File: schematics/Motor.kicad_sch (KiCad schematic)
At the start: 9 parts

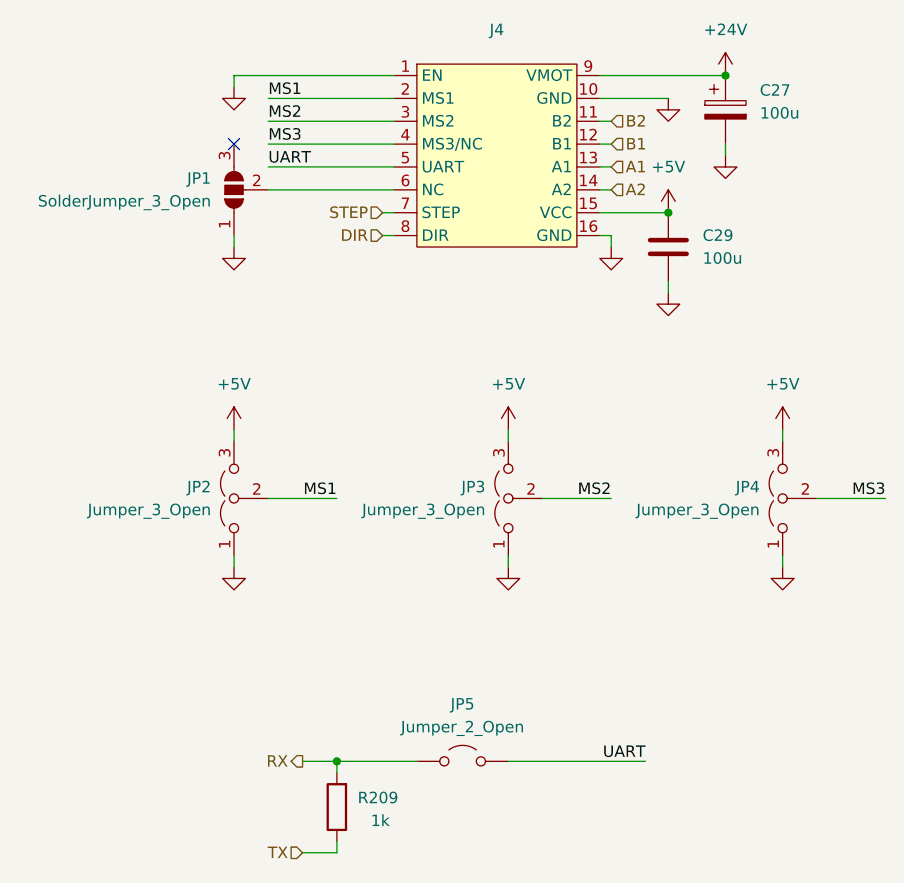
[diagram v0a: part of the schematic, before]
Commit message: Добавил концевик в схему и подправил схему мотора
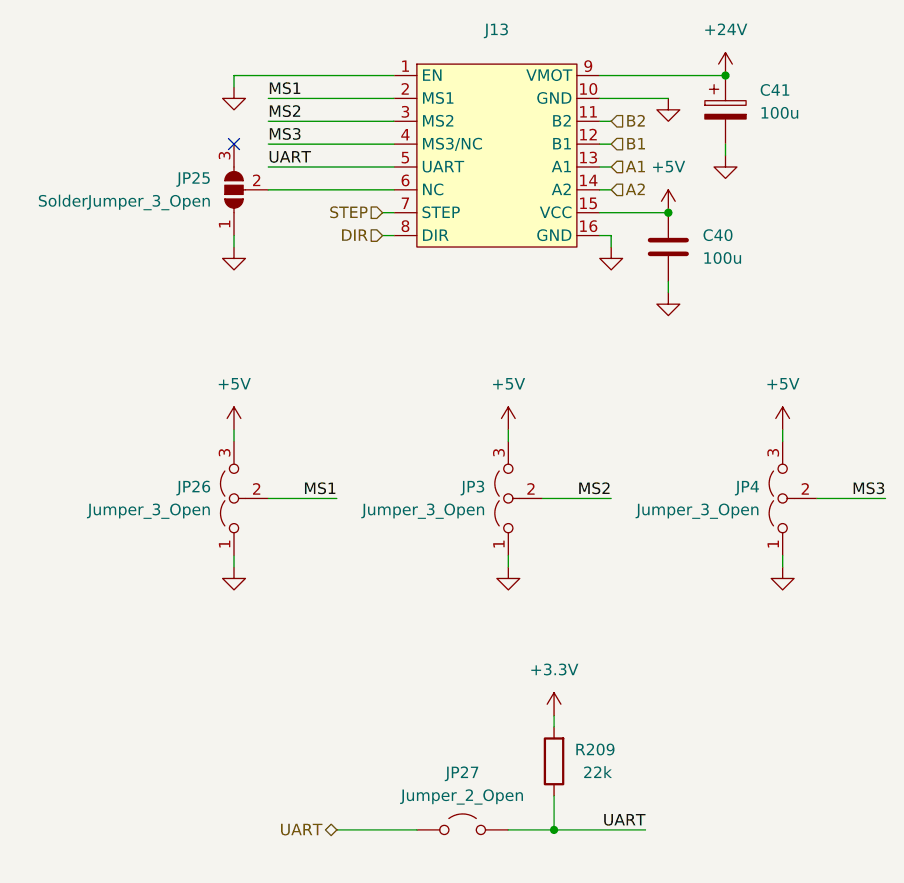
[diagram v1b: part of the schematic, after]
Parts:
- R209: value 1k -> 22k
- renumbered C29 to C40, C27 to C41, J4 to J13, JP1 to JP25, JP2 to JP26, JP5 to JP27
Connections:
- net TX is gone; now on net UART: R209.1
- net UART: now also JP27.1 (A)
- net RX renamed +3.3V
- net +3.3V: no longer JP27.1 (A)
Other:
- moved on the sheet: JP27

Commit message: Файлы измененный Kicad
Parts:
- C40: footprint (none) -> Capacitor_SMD:C_0805_2012Metric
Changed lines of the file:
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@@
 			)
 		)
-		(property "Footprint" ""
+		(property "Footprint" "Capacitor_SMD:C_0805_2012Metric"
 			(at 168.6052 80.01 0)
 			(effects
@@
 		(lib_id "Device:C_Polarized")
 		(at 173.99 60.96 0)
-		(unit 1)
-		(exclude_from_sim no)
-		(in_bom yes)
-		(on_board yes)
-		(dnp no)
-		(fields_autoplaced yes)
+		(mirror y)
+		(unit 1)
+		(exclude_from_sim no)
+		(in_bom yes)
+		(on_board yes)
+		(dnp no)
 		(property "Reference" "C?"
-			(at 177.8 58.8009 0)
+			(at 181.102 58.674 0)
 			(effects
 				(font
@@
 		)
 		(property "Value" "100u"
-			(at 177.8 61.3409 0)
+			(at 182.88 61.468 0)
 			(effects
 				(font
@@
 		)
 		(property "Footprint" "Capacitor_SMD:CP_Elec_6.3x7.7"
-			(at 174.9552 64.77 0)
-			(effects
-				(font
+			(at 173.0248 64.77 0)
+			(effects
+				(font

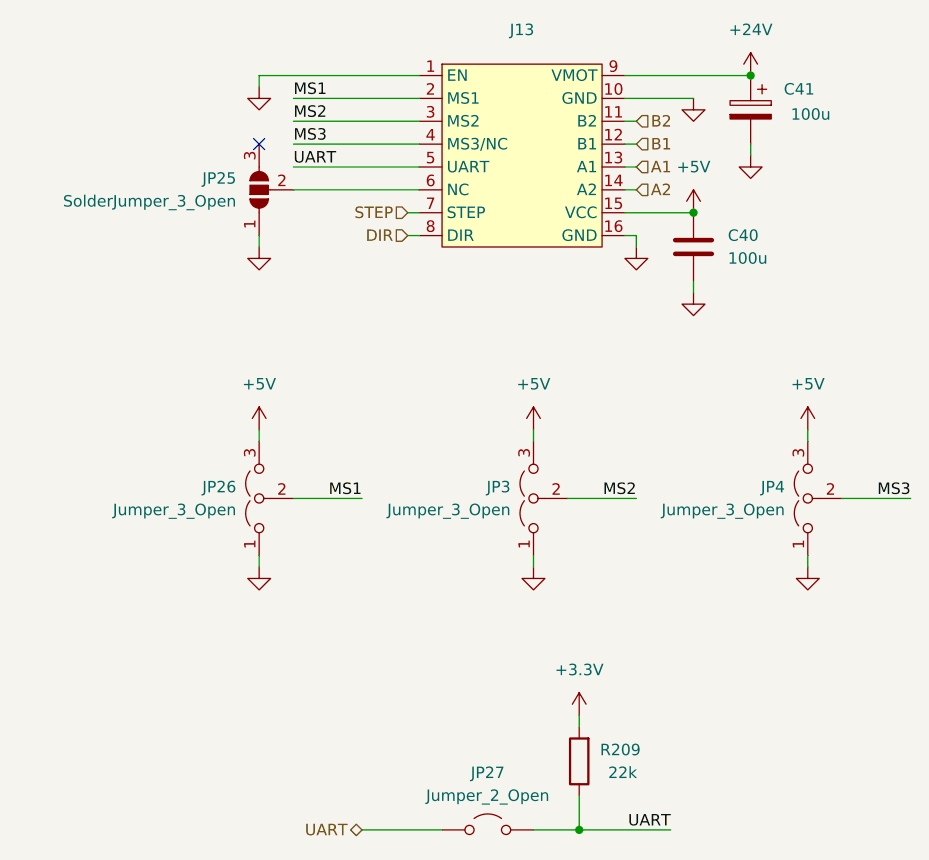
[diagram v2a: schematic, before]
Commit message: Прошелся по всей схеме: 1. почистил компоненты; 2. задал посадочные места; 3. Выставил все ссылки на плате в притык, дальнейшее расширение - смена мк
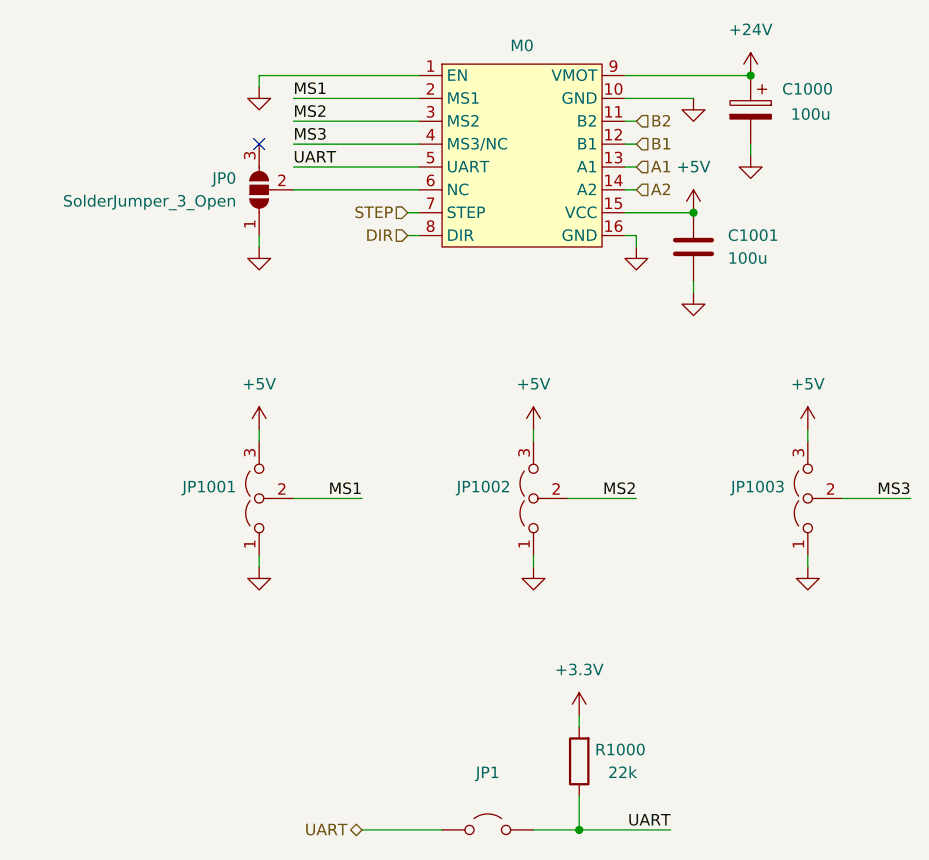
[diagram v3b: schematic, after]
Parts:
- JP1: renamed from JP27; value Jumper_2_Open -> ~
- JP1001: renamed from JP26; value Jumper_3_Open -> ~
- JP1002: renamed from JP3; value Jumper_3_Open -> ~
- JP1003: renamed from JP4; value Jumper_3_Open -> ~
- M0: renamed from J13; footprint (none) -> Library:MotorSocket
- R1000: renamed from R209; footprint Resistor_SMD:R_1206_3216Metric_Pad1.30x1.75mm_HandSolder -> Resistor_SMD:R_0805_2012Metric
- renumbered C41 to C1000, C40 to C1001, JP25 to JP0
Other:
- company: (none) -> Филимонов и К
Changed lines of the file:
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@@
 	(paper "A4")
 	(title_block
+		(company "Филимонов и К")
 		(comment 1 "Мотор")
 		(comment 2 "Филимонов С.В.")
@@
 		(on_board yes)
 		(dnp no)
-		(property "Reference" "R209"
+		(property "Reference" "R1000"
 			(at 159.512 132.08 0)
 			(effects
@@
 			)
 		)
-		(property "Footprint" "Resistor_SMD:R_1206_3216Metric_Pad1.30x1.75mm_HandSolder"
+		(property "Footprint" "Resistor_SMD:R_0805_2012Metric"
 			(at 156.718 133.35 90)
 			(effects
@@
 			(project "MasterBoard"
 				(path "/97e8f341-b455-4614-ab7f-cc310164e7aa/40f863e3-9a2e-4d98-b8ee-4487a1b32b39"
-					(reference "R212")
+					(reference "R1003")
 					(unit 1)
 				)
 				(path "/97e8f341-b455-4614-ab7f-cc310164e7aa/864a8dc6-df84-456c-9a9a-3ea7ad525fa0"
-					(reference "R211")
+					(reference "R1002")
 					(unit 1)
 				)
 				(path "/97e8f341-b455-4614-ab7f-cc310164e7aa/b4807ac2-fff4-43a2-9880-5a7f3b1d6bae"
-					(reference "R210")
+					(reference "R1001")
 					(unit 1)
 				)
 				(path "/97e8f341-b455-4614-ab7f-cc310164e7aa/dcb52573-2c98-48c8-b786-d132966e5cf0"
-					(reference "R209")
+					(reference "R1000")
 					(unit 1)
 				)
@@
 		(dnp no)
 		(fields_autoplaced yes)
-		(property "Reference" "C?"
+		(property "Reference" "C1001"
 			(at 171.45 74.9299 0)
 			(effects
@@
 			(project "MasterBoard"
 				(path "/97e8f341-b455-4614-ab7f-cc310164e7aa/40f863e3-9a2e-4d98-b8ee-4487a1b32b39"
-					(reference "C40")
+					(reference "C1007")
 					(unit 1)
 				)
 				(path "/97e8f341-b455-4614-ab7f-cc310164e7aa/864a8dc6-df84-456c-9a9a-3ea7ad525fa0"
-					(reference "C38")
+					(reference "C1005")
 					(unit 1)
 				)
 				(path "/97e8f341-b455-4614-ab7f-cc310164e7aa/b4807ac2-fff4-43a2-9880-5a7f3b1d6bae"
-					(reference "C36")
+					(reference "C1003")
 					(unit 1)
 				)
 				(path "/97e8f341-b455-4614-ab7f-cc310164e7aa/dcb52573-2c98-48c8-b786-d132966e5cf0"
-					(reference "C?")
+					(reference "C1001")
 					(unit 1)
 				)
@@
 		(dnp no)
 		(fields_autoplaced yes)
-		(property "Reference" "JP?"
+		(property "Reference" "JP1"
 			(at 144.78 134.62 0)
 			(effects
@@
 			)
 		)
-		(property "Value" "Jumper_2_Open"
+		(property "Value" "~"
 			(at 144.78 137.16 0)
 			(effects
@@
 			(project "MasterBoard"
 				(path "/97e8f341-b455-4614-ab7f-cc310164e7aa/40f863e3-9a2e-4d98-b8ee-4487a1b32b39"
-					(reference "JP27")
+					(reference "JP7")
 					(unit 1)
 				)
 				(path "/97e8f341-b455-4614-ab7f-cc310164e7aa/864a8dc6-df84-456c-9a9a-3ea7ad525fa0"
-					(reference "JP24")
+					(reference "JP5")
 					(unit 1)
 				)
 				(path "/97e8f341-b455-4614-ab7f-cc310164e7aa/b4807ac2-fff4-43a2-9880-5a7f3b1d6bae"
-					(reference "JP21")
+					(reference "JP3")
 					(unit 1)
 				)
 				(path "/97e8f341-b455-4614-ab7f-cc310164e7aa/dcb52573-2c98-48c8-b786-d132966e5cf0"
-					(reference "JP?")
+					(reference "JP1")
 					(unit 1)
 				)
@@
 		(on_board yes)
 		(dnp no)
-		(property "Reference" "C?"
-			(at 181.102 58.674 0)
+		(property "Reference" "C1000"
+			(at 183.134 58.674 0)
 			(effects
 				(font
@@
 			(project "MasterBoard"
 				(path "/97e8f341-b455-4614-ab7f-cc310164e7aa/40f863e3-9a2e-4d98-b8ee-4487a1b32b39"
-					(reference "C41")
+					(reference "C1006")
 					(unit 1)
 				)
 				(path "/97e8f341-b455-4614-ab7f-cc310164e7aa/864a8dc6-df84-456c-9a9a-3ea7ad525fa0"
-					(reference "C39")
+					(reference "C1004")
 					(unit 1)
 				)
 				(path "/97e8f341-b455-4614-ab7f-cc310164e7aa/b4807ac2-fff4-43a2-9880-5a7f3b1d6bae"
-					(reference "C37")
+					(reference "C1002")
 					(unit 1)
 				)
 				(path "/97e8f341-b455-4614-ab7f-cc310164e7aa/dcb52573-2c98-48c8-b786-d132966e5cf0"
-					(reference "C?")
+					(reference "C1000")
 					(unit 1)
 				)
@@
 		(on_board yes)
 		(dnp no)
-		(fields_autoplaced yes)
-		(property "Reference" "J?"
-			(at 148.59 52.07 0)
+		(property "Reference" "M0"
+			(at 148.59 53.848 0)
 			(effects
 				(font
@@
 			)
 		)
-		(property "Footprint" ""
+		(property "Footprint" "Library:MotorSocket"
 			(at 148.59 66.04 0)
 			(effects
@@
 			(project "MasterBoard"
 				(path "/97e8f341-b455-4614-ab7f-cc310164e7aa/40f863e3-9a2e-4d98-b8ee-4487a1b32b39"
-					(reference "J13")
+					(reference "M3")
 					(unit 1)
 				)
 				(path "/97e8f341-b455-4614-ab7f-cc310164e7aa/864a8dc6-df84-456c-9a9a-3ea7ad525fa0"
-					(reference "J12")
+					(reference "M2")
 					(unit 1)
 				)
 				(path "/97e8f341-b455-4614-ab7f-cc310164e7aa/b4807ac2-fff4-43a2-9880-5a7f3b1d6bae"
-					(reference "J11")
+					(reference "M1")
 					(unit 1)
 				)
 				(path "/97e8f341-b455-4614-ab7f-cc310164e7aa/dcb52573-2c98-48c8-b786-d132966e5cf0"
-					(reference "J?")
+					(reference "M0")
 					(unit 1)
 				)
@@
 		(dnp no)
 		(fields_autoplaced yes)
-		(property "Reference" "JP3"
+		(property "Reference" "JP1002"
 			(at 147.32 102.8699 90)
 			(effects
@@
 			)
 		)
-		(property "Value" "Jumper_3_Open"
+		(property "Value" "~"
 			(at 147.32 105.4099 90)
 			(effects
@@
 			(project "MasterBoard"
 				(path "/97e8f341-b455-4614-ab7f-cc310164e7aa/40f863e3-9a2e-4d98-b8ee-4487a1b32b39"
-					(reference "JP9")
+					(reference "JP1011")
 					(unit 1)
 				)
 				(path "/97e8f341-b455-4614-ab7f-cc310164e7aa/864a8dc6-df84-456c-9a9a-3ea7ad525fa0"
-					(reference "JP7")
+					(reference "JP1008")
 					(unit 1)
 				)
 				(path "/97e8f341-b455-4614-ab7f-cc310164e7aa/b4807ac2-fff4-43a2-9880-5a7f3b1d6bae"
-					(reference "JP5")
+					(reference "JP1005")
 					(unit 1)
 				)
 				(path "/97e8f341-b455-4614-ab7f-cc310164e7aa/dcb52573-2c98-48c8-b786-d132966e5cf0"
-					(reference "JP3")
+					(reference "JP1002")
 					(unit 1)
 				)
@@
 		(dnp no)
 		(fields_autoplaced yes)
-		(property "Reference" "JP?"
+		(property "Reference" "JP1001"
 			(at 116.84 102.8699 90)
 			(effects
@@
 			)
 		)
-		(property "Value" "Jumper_3_Open"
+		(property "Value" "~"
 			(at 116.84 105.4099 90)
 			(effects
@@
 			(project "MasterBoard"
 				(path "/97e8f341-b455-4614-ab7f-cc310164e7aa/40f863e3-9a2e-4d98-b8ee-4487a1b32b39"
-					(reference "JP26")
+					(reference "JP1010")
 					(unit 1)
 				)
 				(path "/97e8f341-b455-4614-ab7f-cc310164e7aa/864a8dc6-df84-456c-9a9a-3ea7ad525fa0"
-					(reference "JP23")
+					(reference "JP1007")
 					(unit 1)
 				)
 				(path "/97e8f341-b455-4614-ab7f-cc310164e7aa/b4807ac2-fff4-43a2-9880-5a7f3b1d6bae"
-					(reference "JP20")
+					(reference "JP1004")
 					(unit 1)
 				)
 				(path "/97e8f341-b455-4614-ab7f-cc310164e7aa/dcb52573-2c98-48c8-b786-d132966e5cf0"
-					(reference "JP?")
+					(reference "JP1001")
 					(unit 1)
 				)
@@
 		(dnp no)
 		(fields_autoplaced yes)
-		(property "Reference" "JP4"
+		(property "Reference" "JP1003"
 			(at 177.8 102.8699 90)
 			(effects
@@
 			)
 		)
-		(property "Value" "Jumper_3_Open"
+		(property "Value" "~"
 			(at 177.8 105.4099 90)
 			(effects
@@
 			(project "MasterBoard"
 				(path "/97e8f341-b455-4614-ab7f-cc310164e7aa/40f863e3-9a2e-4d98-b8ee-4487a1b32b39"
-					(reference "JP10")
+					(reference "JP1012")
 					(unit 1)
 				)
 				(path "/97e8f341-b455-4614-ab7f-cc310164e7aa/864a8dc6-df84-456c-9a9a-3ea7ad525fa0"
-					(reference "JP8")
+					(reference "JP1009")
 					(unit 1)
 				)
 				(path "/97e8f341-b455-4614-ab7f-cc310164e7aa/b4807ac2-fff4-43a2-9880-5a7f3b1d6bae"
-					(reference "JP6")
+					(reference "JP1006")
 					(unit 1)
 				)
 				(path "/97e8f341-b455-4614-ab7f-cc310164e7aa/dcb52573-2c98-48c8-b786-d132966e5cf0"
-					(reference "JP4")
+					(reference "JP1003")
 					(unit 1)
 				)
@@
 		(dnp no)
 		(fields_autoplaced yes)
-		(property "Reference" "JP?"
+		(property "Reference" "JP0"
 			(at 116.84 68.5799 90)
 			(effects
@@
 			(project "MasterBoard"
 				(path "/97e8f341-b455-4614-ab7f-cc310164e7aa/40f863e3-9a2e-4d98-b8ee-4487a1b32b39"
-					(reference "JP25")
+					(reference "JP6")
 					(unit 1)
 				)
 				(path "/97e8f341-b455-4614-ab7f-cc310164e7aa/864a8dc6-df84-456c-9a9a-3ea7ad525fa0"
-					(reference "JP22")
+					(reference "JP4")
 					(unit 1)
 				)
 				(path "/97e8f341-b455-4614-ab7f-cc310164e7aa/b4807ac2-fff4-43a2-9880-5a7f3b1d6bae"
-					(reference "JP19")
+					(reference "JP2")
 					(unit 1)
 				)
 				(path "/97e8f341-b455-4614-ab7f-cc310164e7aa/dcb52573-2c98-48c8-b786-d132966e5cf0"
-					(reference "JP?")
-					(unit 1)
-				)
+					(reference "JP0")
+					(unit 1)
+				)

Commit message: Не корректно посадочное место выбрал
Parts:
- JP1: footprint Connector_PinHeader_1.00mm:PinHeader_1x02_P1.00mm_Vertical -> Connector_PinHeader_2.54mm:PinHeader_1x02_P2.54mm_Vertical
- JP1001, JP1002, JP1003: footprint Connector_PinHeader_1.00mm:PinHeader_1x03_P1.00mm_Vertical -> Connector_PinHeader_2.54mm:PinHeader_1x03_P2.54mm_Vertical
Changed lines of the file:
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@@
 			)
 		)
-		(property "Footprint" "Connector_PinHeader_1.00mm:PinHeader_1x02_P1.00mm_Vertical"
+		(property "Footprint" "Connector_PinHeader_2.54mm:PinHeader_1x02_P2.54mm_Vertical"
 			(at 144.78 140.97 0)
 			(effects
@@
 			)
 		)
-		(property "Footprint" "Connector_PinHeader_1.00mm:PinHeader_1x03_P1.00mm_Vertical"
+		(property "Footprint" "Connector_PinHeader_2.54mm:PinHeader_1x03_P2.54mm_Vertical"
 			(at 149.86 104.14 0)
 			(effects
@@
 			)
 		)
-		(property "Footprint" "Connector_PinHeader_1.00mm:PinHeader_1x03_P1.00mm_Vertical"
+		(property "Footprint" "Connector_PinHeader_2.54mm:PinHeader_1x03_P2.54mm_Vertical"
 			(at 119.38 104.14 0)
 			(effects
@@
 			)
 		)
-		(property "Footprint" "Connector_PinHeader_1.00mm:PinHeader_1x03_P1.00mm_Vertical"
+		(property "Footprint" "Connector_PinHeader_2.54mm:PinHeader_1x03_P2.54mm_Vertical"
 			(at 180.34 104.14 0)
 			(effects

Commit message: Был косяк в обозначениях
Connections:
- net UART: no longer JP1.2 (B), M0.5 (UART), R1000.1
- new net M_UART: JP1.2 (B), M0.5 (UART), R1000.1
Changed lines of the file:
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@@
 		)
 	)
-	(label "UART"
+	(label "M_UART"
 		(at 123.19 67.31 0)
 		(effects
@@
 			)
 			(justify left bottom)
-		)
-	)
-	(label "UART"
-		(at 165.1 140.97 180)
-		(effects
-			(font
-				(size 1.27 1.27)
-			)
-			(justify right bottom)
 		)
 	)
@@
 		)
 	)
+	(label "M_UART"
+		(at 165.1 140.97 180)
+		(effects
+			(font
+				(size 1.27 1.27)
+			)
+			(justify right bottom)
+		)
+	)
